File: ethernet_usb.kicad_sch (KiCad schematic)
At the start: 22 parts, among them J6 USB_A

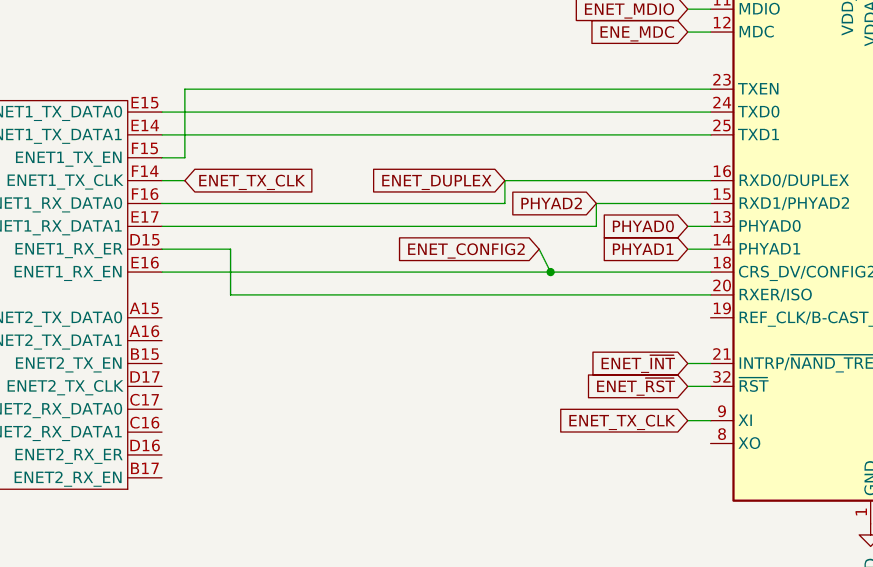
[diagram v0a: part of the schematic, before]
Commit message: Add in on-off switch, power-on reset controller
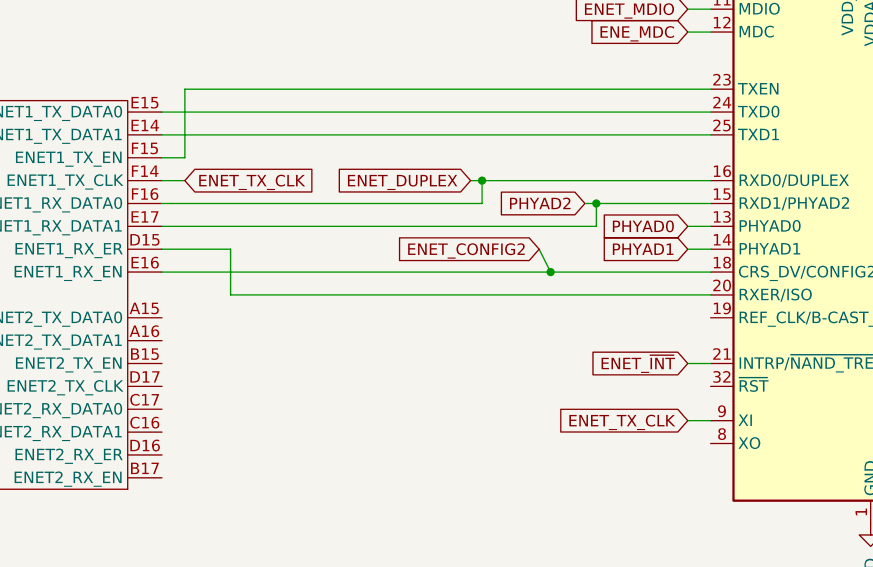
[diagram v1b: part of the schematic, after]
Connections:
- net ENET_~{RST}: no longer names the net of U7.32 (~{RST})

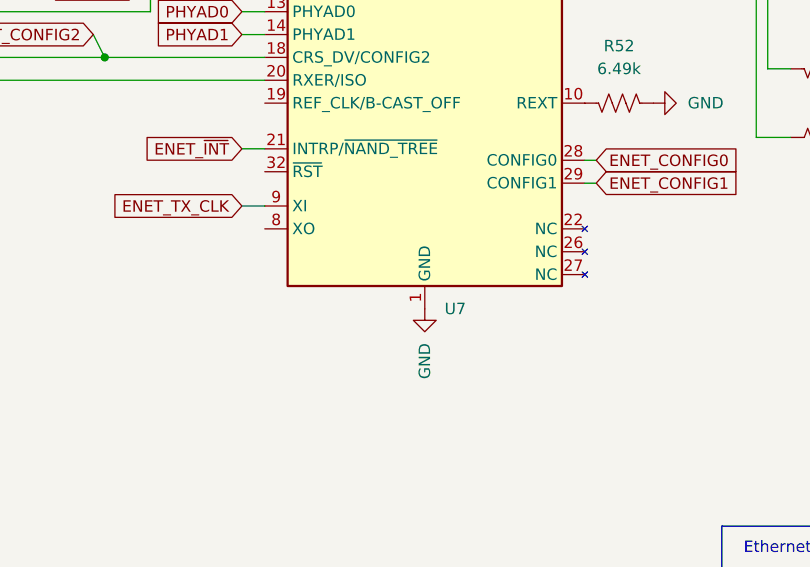
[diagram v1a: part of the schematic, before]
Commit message: Add in LCSC part numbers for major parts, assign packages
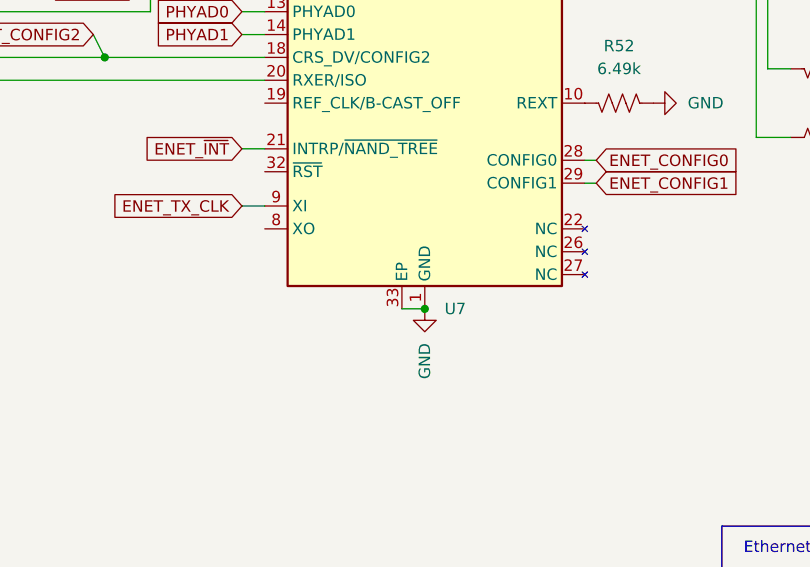
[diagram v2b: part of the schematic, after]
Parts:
- C61, C62, C66, C67, C68, C69, C71: footprint (none) -> Capacitor_SMD:C_0402_1005Metric
- C70: footprint (none) -> Capacitor_SMD:C_0603_1608Metric
- J6: LCSC Part # (none) -> C293351
- R52, R53, R58, R59, R60, R63, R64, R65, R66, R69: footprint (none) -> Resistor_SMD:R_0402_1005Metric
- U1: LCSC Part # (none) -> C414042
- U7: LCSC Part # (none) -> C100018
- U8: LCSC Part # (none) -> C12074
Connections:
- net GND: now also U7.33 (EP)
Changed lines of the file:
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@@
 	(paper "A4")
 	(junction
+		(at 153.67 91.44)
+		(diameter 0)
+		(color 0 0 0 0)
+	)
+	(junction
 		(at 279.4 148.59)
 		(diameter 0)
@@
 	(wire
 		(pts
+			(xy 153.67 91.44) (xy 151.13 91.44)
+		)
+		(stroke
+			(width 0)
+			(type default)
+		)
+	)
+	(wire
+		(pts
 			(xy 95.25 107.95) (xy 81.28 107.95)
 		)
@@
 			)
 		)
-		(property "Footprint" ""
+		(property "Footprint" "Resistor_SMD:R_0402_1005Metric"
 			(at 275.336 134.874 90)
 			(effects
@@
 			)
 		)
-		(property "Footprint" ""
+		(property "Footprint" "Capacitor_SMD:C_0402_1005Metric"
 			(at 38.4048 115.57 0)
 			(effects
@@
 			)
 		)
-		(property "Footprint" ""
+		(property "Footprint" "Resistor_SMD:R_0402_1005Metric"
 			(at 256.794 128.524 90)
 			(effects
@@
 			)
 		)
+		(property "LCSC Part #" "C414042"
+			(at 66.04 120.65 0)
+			(effects
+				(font
+					(size 1.27 1.27)
+				)
+				(hide yes)
+			)
+		)
 		(pin "A6"
 		)
@@
 			)
 		)
-		(property "Footprint" ""
+		(property "Footprint" "Resistor_SMD:R_0402_1005Metric"
 			(at 197.866 63.754 90)
 			(effects
@@
 			)
 		)
-		(property "Footprint" ""
+		(property "Footprint" "Capacitor_SMD:C_0402_1005Metric"
 			(at 203.2 44.7548 0)
 			(effects
@@
 			)
 		)
-		(property "Footprint" ""
+		(property "Footprint" "Capacitor_SMD:C_0402_1005Metric"
 			(at 210.82 32.0548 0)
 			(effects
@@
 			)
 		)
+		(property "LCSC Part #" "C414042"
+			(at 54.61 170.18 0)
+			(effects
+				(font
+					(size 1.27 1.27)
+				)
+				(hide yes)
+			)
+		)
 		(pin "A6"
 		)
@@
 			)
 		)
-		(property "Footprint" ""
+		(property "Footprint" "Capacitor_SMD:C_0402_1005Metric"
 			(at 24.4348 53.34 0)
 			(effects
@@
 			)
 		)
-		(property "Footprint" ""
+		(property "Footprint" "Capacitor_SMD:C_0603_1608Metric"
 			(at 89.2048 181.61 0)
 			(effects
@@
 			)
 		)
+		(property "LCSC Part #" "C414042"
+			(at 53.34 60.96 0)
+			(effects
+				(font
+					(size 1.27 1.27)
+				)
+				(hide yes)
+			)
+		)
 		(pin "A6"
 		)
@@
 			)
 		)
-		(property "Footprint" ""
+		(property "Footprint" "Resistor_SMD:R_0402_1005Metric"
 			(at 264.414 128.524 90)
 			(effects
@@
 			)
 		)
+		(property "LCSC Part #" "C293351"
+			(at 110.49 163.83 0)
+			(effects
+				(font
+					(size 1.27 1.27)
+				)
+				(hide yes)
+			)
+		)
 		(pin "5"
 		)
@@
 			)
 		)
-		(property "Footprint" ""
+		(property "Footprint" "Resistor_SMD:R_0402_1005Metric"
 			(at 275.336 142.494 90)
 			(effects
@@
 			)
 		)
-		(property "Footprint" ""
+		(property "Footprint" "Capacitor_SMD:C_0402_1005Metric"
 			(at 123.4948 21.59 0)
 			(effects
@@
 			)
 		)
-		(property "Footprint" ""
+		(property "Footprint" "Resistor_SMD:R_0402_1005Metric"
 			(at 275.336 147.574 90)
 			(effects
@@
 			)
 		)
+		(property "LCSC Part #" "C100018"
+			(at 153.67 54.61 0)
+			(effects
+				(font
+					(size 1.27 1.27)
+				)
+				(hide yes)
+			)
+		)
 		(pin "9"
 		)
@@
 		(pin "2"
 		)
+		(pin "33"
+		)
 		(instances
 			(project "imx6test"
@@
 			)
 		)
-		(property "Footprint" ""
+		(property "Footprint" "Capacitor_SMD:C_0402_1005Metric"
 			(at 139.3952 21.59 0)
 			(effects
@@
 			)
 		)
-		(property "Footprint" ""
+		(property "Footprint" "Resistor_SMD:R_0402_1005Metric"
 			(at 175.006 67.564 90)
 			(effects
@@
 			)
 		)
-		(property "Footprint" ""
+		(property "Footprint" "Resistor_SMD:R_0402_1005Metric"
 			(at 275.336 145.034 90)
 			(effects
@@
 			)
 		)
-		(property "Footprint" ""
+		(property "Footprint" "Resistor_SMD:R_0402_1005Metric"
 			(at 275.336 137.414 90)
 			(effects
@@
 			)
 		)
-		(property "Footprint" ""
+		(property "Footprint" "Resistor_SMD:R_0402_1005Metric"
 			(at 197.866 73.406 90)
 			(effects
@@
 			)
 		)
+		(property "LCSC Part #" "C12074"
+			(at 231.14 49.53 0)
+			(effects
+				(font
+					(size 1.27 1.27)
+				)
+				(hide yes)
+			)
+		)
 		(pin "8"
 		)
@@
 			)
 		)
-		(property "Footprint" ""
+		(property "Footprint" "Capacitor_SMD:C_0402_1005Metric"
 			(at 101.9048 181.61 0)
 			(effects
